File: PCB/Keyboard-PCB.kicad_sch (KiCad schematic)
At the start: 53 parts, among them J1 USB_C_Receptacle_USB2.0_16P, J2 USB_C_Receptacle_USB2.0_16P, SW1 SW_Push, SW10 SW_Push, SW11 SW_Push, SW12 SW_Push, SW13 SW_Push, SW14 SW_Push, SW15 SW_Push, SW16 SW_Push, SW17 SW_Push, SW18 SW_Push, SW19 SW_Push, SW2 SW_Push, SW20 SW_Push, SW21 SW_Push, SW3 SW_Push, SW4 SW_Push, SW5 SW_Push, SW6 SW_Push, SW7 SW_Push, SW8 SW_Push, SW9 SW_Push, U1 AMS1117-3.3, U2 STM32WB55CCUx

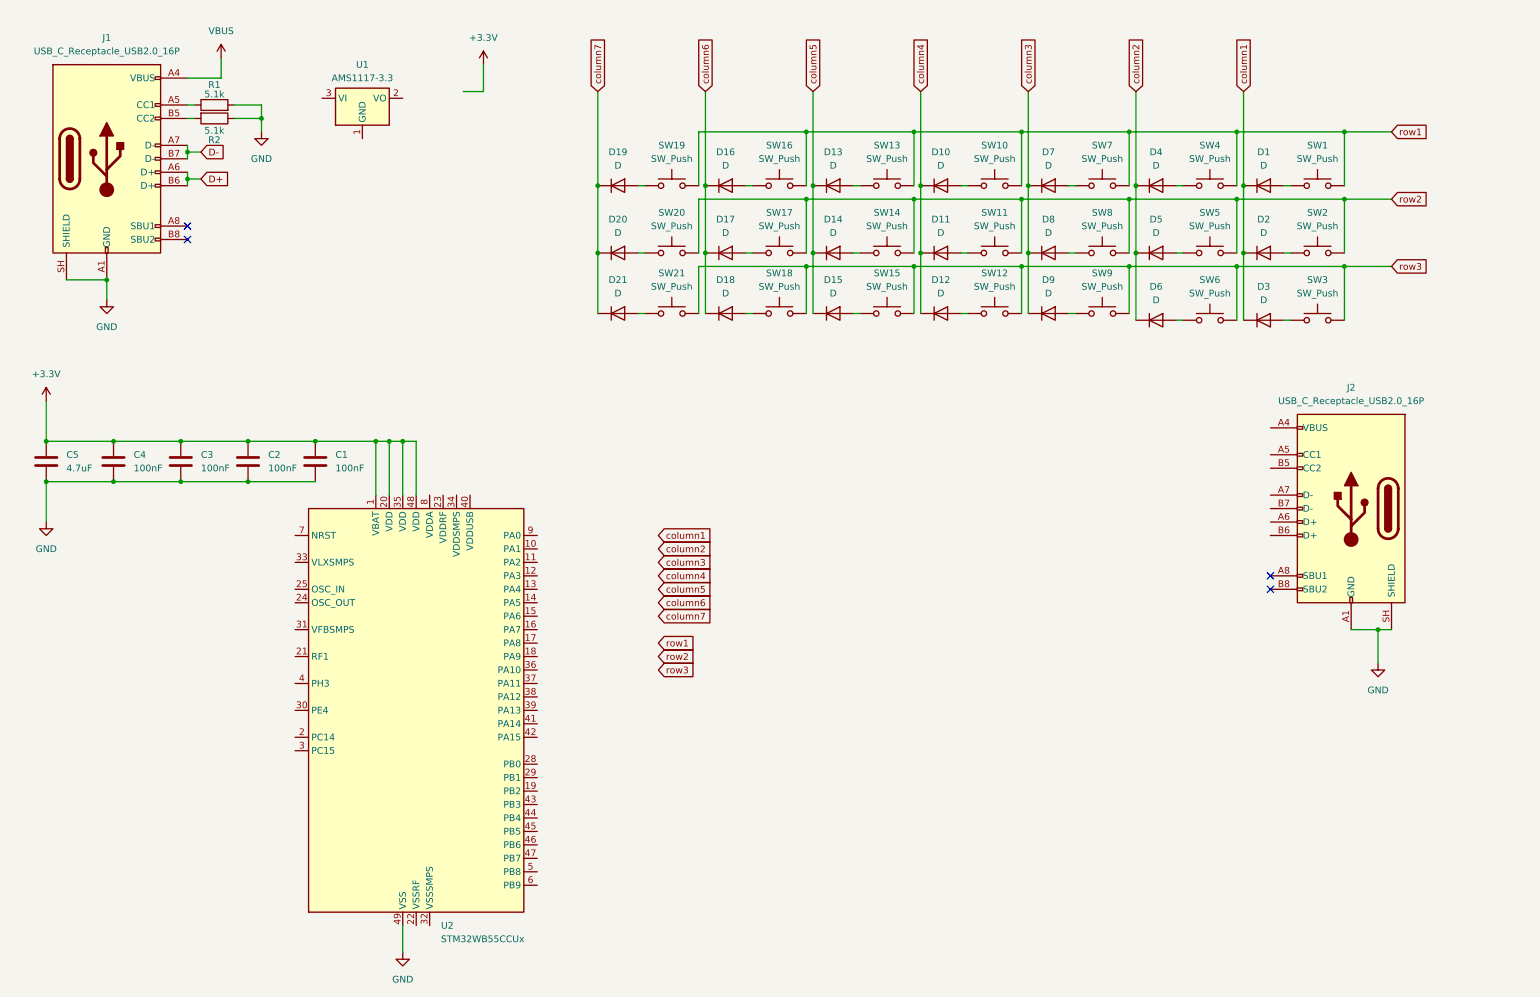
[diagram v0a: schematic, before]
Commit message: new hotswap footprints and adjustments
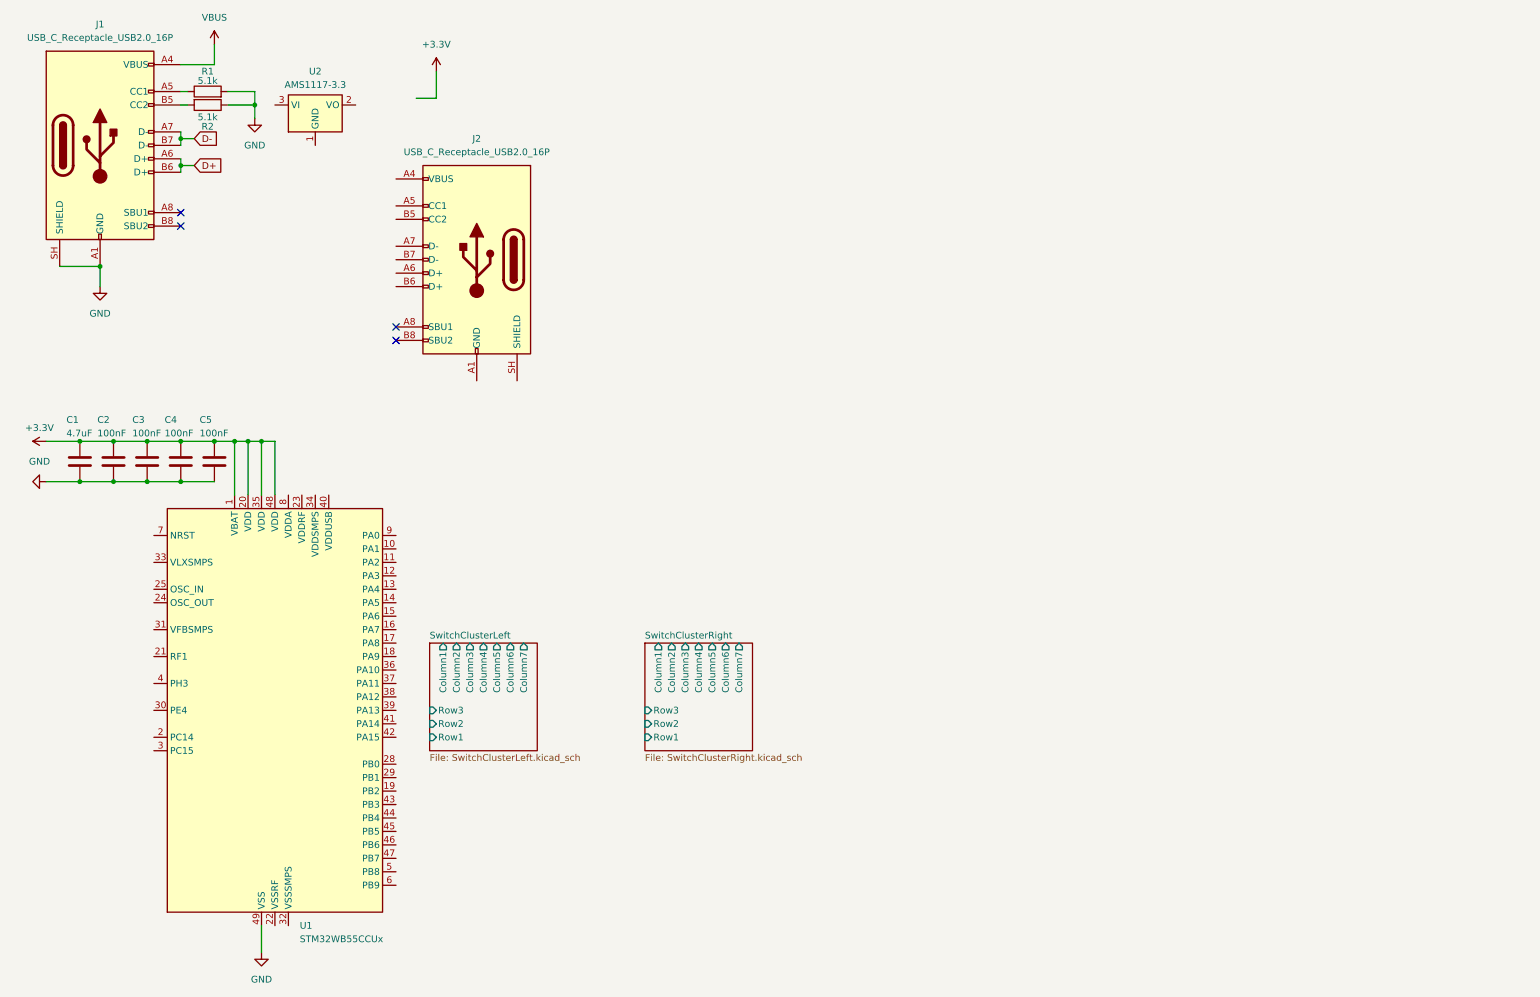
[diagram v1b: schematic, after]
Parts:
- removed D1, D10, D11, D12, D13, D14, D15, D16, D17, D18, D19, D2, D20, D21, D3, D4, D5, D6, D7, D8, D9: D, Diode_SMD:Nexperia_CFP3_SOD-123W, symbol Device:D
- removed SW1, SW10, SW11, SW12, SW13, SW14, SW15, SW16, SW17, SW18, SW19, SW2, SW20, SW21, SW3, SW4, SW5, SW6, SW7, SW8, SW9: SW_Push, Button_Switch_Keyboard:SW_Cherry_MX_1.00u_PCB, symbol Switch:SW_Push
- renumbered C5 to C1, C4 to C2, C2 to C4, C1 to C5, U2 to U1, U1 to U2
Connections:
- net GND: no longer J2.A1 (GND), J2.A12 (GND), J2.B1 (GND), J2.B12 (GND), J2.SH (SHIELD)
- new net: J2.A1 (GND), J2.A12 (GND), J2.B1 (GND), J2.B12 (GND)
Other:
- added sheet SwitchClusterLeft (SwitchClusterLeft.kicad_sch)
- added sheet SwitchClusterRight (SwitchClusterRight.kicad_sch)
- moved on the sheet: C1, C3, C4, C5, J1, J2, R1, R2, U1, U2

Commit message: Basic Component Placement
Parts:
- removed J2: USB_C_Receptacle_USB2.0_16P, Connector_USB:USB_C_Receptacle_GCT_USB4085, symbol Connector:USB_C_Receptacle_USB2.0_16P
- removed U1: STM32WB55CCUx, Package_DFN_QFN:QFN-48-1EP_7x7mm_P0.5mm_EP5.6x5.6mm, symbol MCU_ST_STM32WB:STM32WB55CCUx
- added C10, C11, C12, C15, C16, C7, C8, C9: 100nF, Capacitor_SMD:C_0402_1005Metric, symbol Device:C
- added C13, C17: 1uF, Capacitor_SMD:C_0402_1005Metric, symbol Device:C
- added C14, C18: 100n, Capacitor_SMD:C_0402_1005Metric, symbol Device:C
- added C19, C20, C21, C22: 0.1uF, Capacitor_SMD:C_0402_1005Metric, symbol Device:C
- added C6: 4.7uF, Capacitor_SMD:C_0402_1005Metric, symbol Device:C
- added D43: SP0503BAHT, Package_TO_SOT_SMD:SOT-143, symbol Power_Protection:SP0503BAHT
- added J2, J7: AudioJack4, MyLibrary:Jack_3.5mm_CUI_SJ1-3524N_Horizontal, symbol Connector_Audio:AudioJack4
- added J3, J5: BOOT0, Connector_PinHeader_2.54mm:PinHeader_1x03_P2.54mm_Vertical, symbol Connector:Conn_01x03_Pin
- added J4, J6: BOOT1, Connector_PinHeader_2.54mm:PinHeader_1x03_P2.54mm_Vertical, symbol Connector:Conn_01x03_Pin
- added R5, R6, R7, R8: 10k, Resistor_SMD:R_0805_2012Metric, symbol Device:R
- added SW43, SW45: SW_Push, Button_Switch_SMD:SW_Push_1P1T_NO_CK_KMR2, symbol Switch:SW_Push
- added U1, U3: STM32F103C6Tx, Package_QFP:LQFP-48_7x7mm_P0.5mm, symbol MCU_ST_STM32F1:STM32F103C6Tx
- C1: value 4.7uF -> 10uF; footprint (none) -> Capacitor_SMD:C_0402_1005Metric
- C2, C3, C4, C5: footprint (none) -> Capacitor_SMD:C_0402_1005Metric
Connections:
- net +3.3V: now also U2.2 (VO), C10.1, C11.1, C12.1, C13.1, C15.1, C16.1, C17.1, C20.1, C21.1, C6.1, C7.1, C8.1, C9.1, J2.T, J3.1 (Pin_1), J4.1 (Pin_1), J5.1 (Pin_1), J6.1 (Pin_1), J7.T, U1.1 (VBAT), U1.24 (VDD), U1.36 (VDD), U1.48 (VDD), U1.9 (VDDA), U3.1 (VBAT), U3.24 (VDD), U3.36 (VDD), U3.48 (VDD), U3.9 (VDDA)
- net D+: now also D43.4 (K)
- net D-: now also D43.3 (K)
- net GND: now also U2.1 (GND), C10.2, C11.2, C12.2, C13.2, C14.2, C15.2, C16.2, C17.2, C18.2, C19.2, C20.2, C21.2, C22.2, C6.2, C7.2, C8.2, C9.2, D43.1 (A), J2.S, J3.3 (Pin_3), J4.3 (Pin_3), J5.3 (Pin_3), J6.3 (Pin_3), J7.S, SW43.1, SW45.1, U1.23 (VSS), U1.35 (VSS), U1.47 (VSS), U1.8 (VSSA), U3.23 (VSS), U3.35 (VSS), U3.47 (VSS), U3.8 (VSSA)
- net VBUS: now also U2.3 (VI), C19.1, C22.1, D43.2 (K)
- new net BOOT0: R5.2, R7.2, U1.44 (BOOT0), U3.44 (BOOT0)
- new net BOOT0R: J3.2 (Pin_2), J5.2 (Pin_2), R5.1, R7.1
- new net BOOT1: R6.2, R8.2, U1.20 (PB2), U3.20 (PB2)
- new net BOOT1R: J4.2 (Pin_2), J6.2 (Pin_2), R6.1, R8.1
- new net NRST: C14.1, C18.1, SW43.2, SW45.2, U1.7 (NRST), U3.7 (NRST)
- no-connect marks 4 -> 2
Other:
- moved on the sheet: C1, C2, C3, C4, C5, R1, R2, U2

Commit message: Routing Work
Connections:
- net SwitchClusterLeft/Column1: now also U1.16 (PA6)
- net SwitchClusterLeft/Column2: now also U1.15 (PA5)
- net SwitchClusterLeft/Column3: now also U1.14 (PA4)
- net SwitchClusterLeft/Column4: now also U1.13 (PA3)
- net SwitchClusterLeft/Column5: now also U1.12 (PA2)
- net SwitchClusterLeft/Column6: now also U1.11 (PA1)
- net SwitchClusterLeft/Column7: now also U1.10 (PA0)
- net SwitchClusterRight/Column1: now also U3.16 (PA6)
- net SwitchClusterRight/Column2: now also U3.15 (PA5)
- net SwitchClusterRight/Column3: now also U3.14 (PA4)
- net SwitchClusterRight/Column4: now also U3.13 (PA3)
- net SwitchClusterRight/Column5: now also U3.12 (PA2)
- net SwitchClusterRight/Column6: now also U3.11 (PA1)
- net SwitchClusterRight/Column7: now also U3.10 (PA0)
- net SwitchClusterRight/Row1: now also U3.38 (PA15)
- net SwitchClusterRight/Row2: now also U3.37 (PA14)
- net SwitchClusterRight/Row3: now also U3.34 (PA13)
- net at U1.37 (PA14): now also J2.R2
- net at U1.38 (PA15): now also J2.R1
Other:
- note added: "Need to check what pins are UART"
- note added: "Need to check what pins are USB"
- moved on the sheet: J2, J7

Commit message: add some status LEDS and other stuff to schematic
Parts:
- added D44, D45, D46, D47: LED, symbol Device:LED
- added J8, J9: Debug UART, symbol Connector:Conn_01x04_Pin
- added R10, R3, R4, R9: 100R, symbol Device:R
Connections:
- net +3.3V: now also D44.2 (A), D45.2 (A), J8.4 (Pin_4), J9.4 (Pin_4)
- net D+: now also U1.33 (PA12)
- net D-: now also U1.32 (PA11)
- net GND: now also J8.1 (Pin_1), J9.1 (Pin_1), R10.2, R3.2, R4.2, R9.2
- net SwitchClusterLeft/Row1: now also U1.38 (PA15)
- net SwitchClusterLeft/Row2: now also U1.37 (PA14)
- net SwitchClusterLeft/Row3: now also U1.34 (PA13)
- net at U1.2 (PC13): now also D46.2 (A)
- net TX: now reaches U1.30 (PA9)
- net TX: now also J2.R2, J8.2 (Pin_2)
- net RX: now reaches U1.31 (PA10)
- net RX: now also J2.R1, J8.3 (Pin_3)
- net at U3.2 (PC13): now also D47.2 (A)
- net at U3.30 (PA9): now also J7.R2, J9.2 (Pin_2)
- net at U3.31 (PA10): now also J7.R1, J9.3 (Pin_3)
- new net: D47.1 (K), R10.1
- new net: D46.1 (K), R9.1
- new net: D45.1 (K), R4.1
- new net: D44.1 (K), R3.1
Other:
- note added: "Flip these?"
- note removed: "Need to check what pins are UART"
- note removed: "Need to check what pins are USB"
- moved on the sheet: J2, J5, J7

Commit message: more routing
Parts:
- D44, D45, D46, D47: footprint (none) -> LED_SMD:LED_0805_2012Metric
- J8, J9: footprint (none) -> Connector_PinHeader_2.54mm:PinHeader_1x04_P2.54mm_Vertical
- R10, R3, R4, R9: footprint (none) -> Resistor_SMD:R_0402_1005Metric
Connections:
- net PC13: now reaches D46.2 (A), U1.2 (PC13)
- net PC13: now also D47.2 (A), U3.2 (PC13)
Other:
- moved on the sheet: D46, D47, R10, R9
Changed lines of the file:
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@@
 	(wire
 		(pts
-			(xy 204.47 96.52) (xy 205.74 96.52)
+			(xy 203.2 96.52) (xy 205.74 96.52)
 		)
 		(stroke
@@
 	(wire
 		(pts
-			(xy 58.42 129.54) (xy 59.69 129.54)
+			(xy 57.15 129.54) (xy 59.69 129.54)
 		)
 		(stroke
@@
 	(wire
 		(pts
-			(xy 50.8 129.54) (xy 48.26 129.54)
+			(xy 49.53 129.54) (xy 46.99 129.54)
 		)
 		(stroke
@@
 	(wire
 		(pts
-			(xy 196.85 96.52) (xy 194.31 96.52)
+			(xy 195.58 96.52) (xy 193.04 96.52)
 		)
 		(stroke
@@
 	(wire
 		(pts
-			(xy 40.64 129.54) (xy 38.1 129.54)
+			(xy 39.37 129.54) (xy 38.1 129.54)
 		)
 		(stroke
@@
 	(wire
 		(pts
-			(xy 186.69 96.52) (xy 184.15 96.52)
+			(xy 185.42 96.52) (xy 184.15 96.52)
 		)
 		(stroke
@@
 		)
 	)
+	(label "PC13"
+		(at 59.69 129.54 180)
+		(effects
+			(font
+				(size 1.27 1.27)
+			)
+			(justify right bottom)
+		)
+	)
 	(label "NRST"
 		(at 200.66 78.74 0)
@@
 		)
 	)
+	(label "PC13"
+		(at 205.74 96.52 180)
+		(effects
+			(font
+				(size 1.27 1.27)
+			)
+			(justify right bottom)
+		)
+	)
 	(label "NRST"
 		(at 46.99 111.76 0)
@@
 	(symbol
 		(lib_id "Device:R")
-		(at 190.5 96.52 270)
+		(at 189.23 96.52 270)
 		(unit 1)
 		(body_style 1)
@@
 		(dnp no)
 		(property "Reference" "R10"
-			(at 189.23 94.488 90)
+			(at 187.96 94.488 90)
 			(show_name no)
 			(do_not_autoplace no)
@@
 		)
 		(property "Value" "100R"
-			(at 187.96 98.806 90)
+			(at 186.69 98.806 90)
 			(show_name no)
 			(do_not_autoplace no)
@@
 			)
 		)
-		(property "Footprint" ""
-			(at 190.5 94.742 90)
+		(property "Footprint" "Resistor_SMD:R_0402_1005Metric"
+			(at 189.23 94.742 90)
 			(hide yes)
 			(show_name no)
@@
 		)
 		(property "Datasheet" ""
-			(at 190.5 96.52 0)
+			(at 189.23 96.52 0)
 			(hide yes)
 			(show_name no)
@@
 		)
 		(property "Description" "Resistor"
-			(at 190.5 96.52 0)
+			(at 189.23 96.52 0)
 			(hide yes)
 			(show_name no)
@@
 	(symbol
 		(lib_id "Device:LED")
-		(at 54.61 129.54 0)
+		(at 53.34 129.54 0)
 		(unit 1)
 		(body_style 1)
@@
 		(dnp no)
 		(property "Reference" "D46"
-			(at 56.896 133.35 0)
+			(at 55.626 133.35 0)
 			(show_name no)
 			(do_not_autoplace no)
@@
 		)
 		(property "Value" "LED"
-			(at 52.578 133.35 0)
+			(at 51.308 133.35 0)
 			(show_name no)
 			(do_not_autoplace no)
@@
 			)
 		)
-		(property "Footprint" ""
-			(at 54.61 129.54 0)
+		(property "Footprint" "LED_SMD:LED_0805_2012Metric"
+			(at 53.34 129.54 0)
 			(hide yes)
 			(show_name no)
@@
 		)
 		(property "Datasheet" ""
-			(at 54.61 129.54 0)
+			(at 53.34 129.54 0)
 			(hide yes)
 			(show_name no)
@@
 		)
 		(property "Description" "Light emitting diode"
-			(at 54.61 129.54 0)
+			(at 53.34 129.54 0)
 			(hide yes)
 			(show_name no)
@@
 		)
 		(property "Sim.Pins" "1=K 2=A"
-			(at 54.61 129.54 0)
+			(at 53.34 129.54 0)
 			(hide yes)
 			(show_name no)
@@
 			)
 		)
-		(property "Footprint" ""
+		(property "Footprint" "LED_SMD:LED_0805_2012Metric"
 			(at 152.4 29.21 0)
 			(hide yes)
@@
 			)
 		)
-		(property "Footprint" ""
+		(property "Footprint" "Resistor_SMD:R_0402_1005Metric"
 			(at 150.622 40.64 90)
 			(hide yes)
@@
 	(symbol
 		(lib_id "Device:LED")
-		(at 200.66 96.52 0)
+		(at 199.39 96.52 0)
 		(unit 1)
 		(body_style 1)
@@
 		(dnp no)
 		(property "Reference" "D47"
-			(at 202.946 100.33 0)
+			(at 201.676 100.33 0)
 			(show_name no)
 			(do_not_autoplace no)
@@
 		)
 		(property "Value" "LED"
-			(at 198.628 100.33 0)
+			(at 197.358 100.33 0)
 			(show_name no)
 			(do_not_autoplace no)
@@
 			)
 		)
-		(property "Footprint" ""
-			(at 200.66 96.52 0)
+		(property "Footprint" "LED_SMD:LED_0805_2012Metric"
+			(at 199.39 96.52 0)
 			(hide yes)
 			(show_name no)
@@
 		)
 		(property "Datasheet" ""
-			(at 200.66 96.52 0)
+			(at 199.39 96.52 0)
 			(hide yes)
 			(show_name no)
@@
 		)
 		(property "Description" "Light emitting diode"
-			(at 200.66 96.52 0)
+			(at 199.39 96.52 0)
 			(hide yes)
 			(show_name no)
@@
 		)
 		(property "Sim.Pins" "1=K 2=A"
-			(at 200.66 96.52 0)
+			(at 199.39 96.52 0)
 			(hide yes)
 			(show_name no)
@@
 	(symbol
 		(lib_id "Device:R")
-		(at 44.45 129.54 270)
+		(at 43.18 129.54 270)
 		(unit 1)
 		(body_style 1)
@@
 		(dnp no)
 		(property "Reference" "R9"
-			(at 43.18 127.508 90)
+			(at 41.91 127.508 90)
 			(show_name no)
 			(do_not_autoplace no)
@@
 		)
 		(property "Value" "100R"
-			(at 41.91 131.826 90)
+			(at 40.64 131.826 90)
 			(show_name no)
 			(do_not_autoplace no)
@@
 			)
 		)
-		(property "Footprint" ""
-			(at 44.45 127.762 90)
+		(property "Footprint" "Resistor_SMD:R_0402_1005Metric"
+			(at 43.18 127.762 90)
 			(hide yes)
 			(show_name no)
@@
 		)
 		(property "Datasheet" ""
-			(at 44.45 129.54 0)
+			(at 43.18 129.54 0)
 			(hide yes)
 			(show_name no)
@@
 		)
 		(property "Description" "Resistor"
-			(at 44.45 129.54 0)
+			(at 43.18 129.54 0)
 			(hide yes)
 			(show_name no)
@@
 			)
 		)
-		(property "Footprint" ""
+		(property "Footprint" "LED_SMD:LED_0805_2012Metric"
 			(at 139.7 29.21 0)
 			(hide yes)
@@
 			)
 		)
-		(property "Footprint" ""
+		(property "Footprint" "Connector_PinHeader_2.54mm:PinHeader_1x04_P2.54mm_Vertical"
 			(at 242.57 133.35 0)
 			(hide yes)
@@
 			)
 		)
-		(property "Footprint" ""
+		(property "Footprint" "Resistor_SMD:R_0402_1005Metric"
 			(at 137.922 40.64 90)
 			(hide yes)
@@
 			)
 		)
-		(property "Footprint" ""
+		(property "Footprint" "Connector_PinHeader_2.54mm:PinHeader_1x04_P2.54mm_Vertical"
 			(at 99.06 168.91 0)
 			(hide yes)

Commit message: routing done
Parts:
- removed J2, J7: AudioJack4, MyLibrary:Jack_3.5mm_CUI_SJ1-3524N_Horizontal, symbol Connector_Audio:AudioJack4
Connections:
- net RX_S: now reaches J9.2 (Pin_2)
- net RX_S: now also U3.31 (PA10); no longer U3.30 (PA9)
- net TX_S: now reaches J9.3 (Pin_3)
- net TX_S: now also U3.30 (PA9); no longer U3.31 (PA10)
- net BOOT0 renamed BOOT0_M
- net BOOT0_M: no longer R7.2, U3.44 (BOOT0)
- net BOOT0R renamed BOOT0R_M
- net BOOT0R_M: no longer J5.2 (Pin_2), R7.1
- net BOOT1 renamed BOOT1_M
- net BOOT1_M: no longer R8.2, U3.20 (PB2)
- net BOOT1R renamed BOOT1R_M
- net BOOT1R_M: no longer J6.2 (Pin_2), R8.1
- net NRST renamed NRST_M
- net NRST_M: no longer C18.1, SW43.2, U3.7 (NRST)
- net PC13 renamed PC13_M
- net PC13_M: no longer D47.2 (A), U3.2 (PC13)
- net RX renamed RX_M
- net TX renamed TX_M
- new net BOOT0R_S: J5.2 (Pin_2), R7.1
- new net BOOT0_S: R7.2, U3.44 (BOOT0)
- new net BOOT1R_S: J6.2 (Pin_2), R8.1
- new net BOOT1_S: R8.2, U3.20 (PB2)
- new net NRST_S: C18.1, SW43.2, U3.7 (NRST)
- new net PC13_S: D47.2 (A), U3.2 (PC13)
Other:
- note added: "Future Audio Jack"
- note removed: "Flip these?"

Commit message: fix rule checker errors and make BOM
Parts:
- removed U1, U3: STM32F103C6Tx, Package_QFP:LQFP-48_7x7mm_P0.5mm, symbol MCU_ST_STM32F1:STM32F103C6Tx
- added H1, H2, H3, H4: MountingHole, symbol Mechanical:MountingHole
- added U2, U3: STM32F103C8Tx, Package_QFP:LQFP-48_7x7mm_P0.5mm, symbol MCU_ST_STM32F1:STM32F103C8Tx
- C13: renamed from C18; value 100n -> 100nF
- C14: value 100n -> 100nF
- renumbered C13 to C18, C6 to C2, C2 to C6, J3 to J2, J4 to J3, J5 to J4, J6 to J5, J8 to J6, J9 to J7, R6 to R10, R9 to R5, R10 to R6, R5 to R9, SW45 to SW44, U2 to U1
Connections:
- net +3.3V: now also U2.1 (VBAT), U2.24 (VDD), U2.36 (VDD), U2.48 (VDD), U2.9 (VDDA), U3.1 (VBAT), U3.24 (VDD), U3.36 (VDD), U3.48 (VDD), U3.9 (VDDA)
- net BOOT0_M: now also U2.44 (BOOT0)
- net BOOT0_S: now also U3.44 (BOOT0)
- net BOOT1_M: now also U2.20 (PB2)
- net BOOT1_S: now also U3.20 (PB2)
- net D+: now also U2.33 (PA12)
- net D-: now also U2.32 (PA11)
- net GND: now also U2.23 (VSS), U2.35 (VSS), U2.47 (VSS), U2.8 (VSSA), U3.23 (VSS), U3.35 (VSS), U3.47 (VSS), U3.8 (VSSA)
- net NRST_M: now also U2.7 (NRST)
- net NRST_S: now also U3.7 (NRST)
- net PC13_M: now also U2.2 (PC13)
- net PC13_S: now also U3.2 (PC13)
- net RX_M: now also U2.31 (PA10)
- net RX_S: now also U3.31 (PA10)
- net SwitchClusterLeft/Column1: now also U2.16 (PA6)
- net SwitchClusterLeft/Column2: now also U2.15 (PA5)
- net SwitchClusterLeft/Column3: now also U2.14 (PA4)
- net SwitchClusterLeft/Column4: now also U2.13 (PA3)
- net SwitchClusterLeft/Column5: now also U2.12 (PA2)
- net SwitchClusterLeft/Column6: now also U2.11 (PA1)
- net SwitchClusterLeft/Column7: now also U2.10 (PA0)
- net SwitchClusterLeft/Row1: now also U2.38 (PA15)
- net SwitchClusterLeft/Row2: now also U2.37 (PA14)
- net SwitchClusterLeft/Row3: now also U2.34 (PA13)
- net SwitchClusterRight/Column1: now also U3.16 (PA6)
- net SwitchClusterRight/Column2: now also U3.15 (PA5)
- net SwitchClusterRight/Column3: now also U3.14 (PA4)
- net SwitchClusterRight/Column4: now also U3.13 (PA3)
- net SwitchClusterRight/Column5: now also U3.12 (PA2)
- net SwitchClusterRight/Column6: now also U3.11 (PA1)
- net SwitchClusterRight/Column7: now also U3.10 (PA0)
- net SwitchClusterRight/Row1: now also U3.38 (PA15)
- net SwitchClusterRight/Row2: now also U3.37 (PA14)
- net SwitchClusterRight/Row3: now also U3.34 (PA13)
- net TX_M: now also U2.30 (PA9)
- net TX_S: now also U3.30 (PA9)
- no-connect marks 2 -> 54

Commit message: Add mount holes n stuff
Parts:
- added H5, H6, H7, H8: MountingHole, MountingHole:MountingHole_3mm, symbol Mechanical:MountingHole
- H1, H2, H3, H4: footprint (none) -> MountingHole:MountingHole_3mm
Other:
- moved on the sheet: H1, H2, H3, H4
